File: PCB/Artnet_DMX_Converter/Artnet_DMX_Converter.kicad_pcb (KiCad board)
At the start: 4 copper layers, 100 x 72 mm, 208 parts, among them IC1 NPM1300-QEAA-R7, J1 Conn_01x03_MountingPin, J10 XLR5, J11 XLR3, J12 IDC, J13 Conn_02x04, J2 USB_C_Receptacle_USB2.0_14P, J3 RJ45, J4 XLR5, J5 XLR3, J6 XLR5, J7 XLR3, J8 XLR5, J9 XLR3, SW1 SW_Push, SW2 SW_Push, T1 FA2805, U1 RP2350B, U10 MAX3485, U11 MAX3485, U12 TXS0101DCK, U2 W25Q128JVS, U3 USBLC6-2SC6, U4 W5500, U5 VO618A-3X019T, U6 SI3402-B-GMR, U7 TLV431, U8 MAX3485, U9 MAX3485, Y1 ABM8-272-T3, Y2 ABM8-25.000MHZ-10-D1G-T

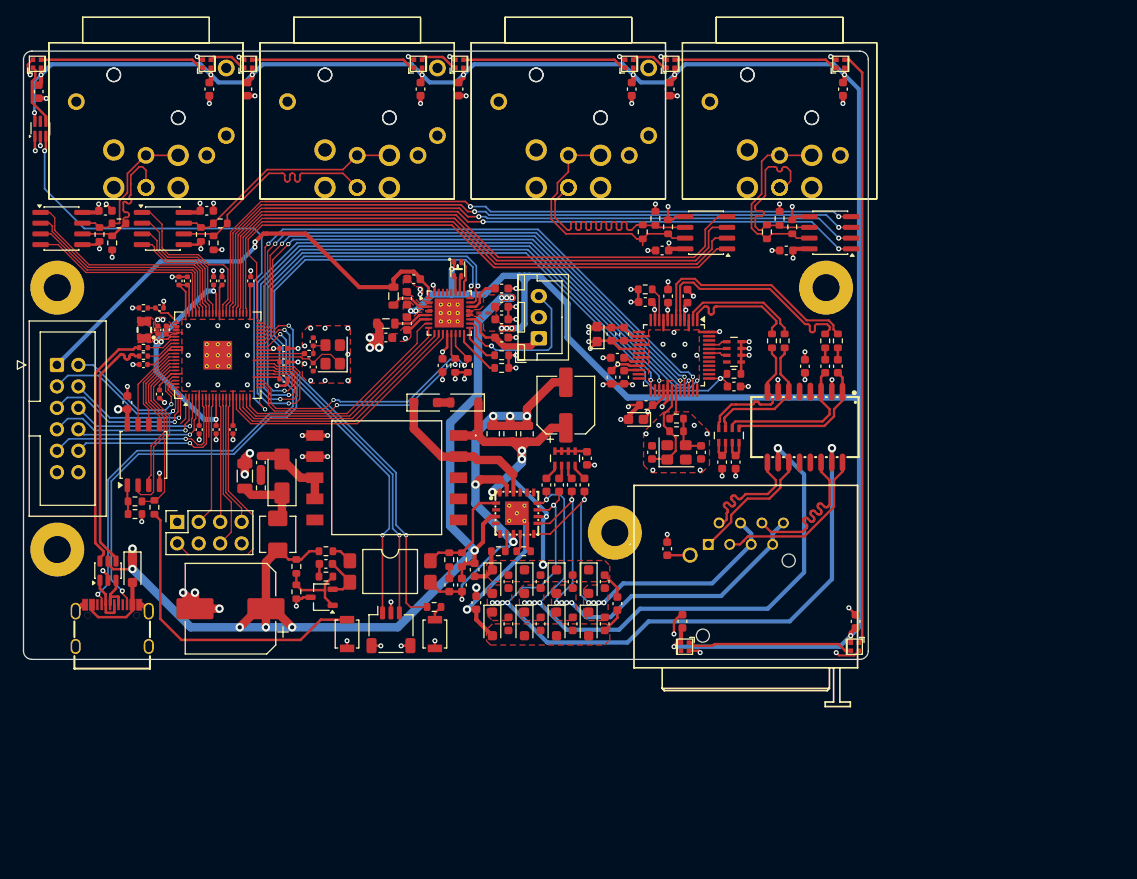
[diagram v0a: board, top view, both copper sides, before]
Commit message: Updated the PCB Allot
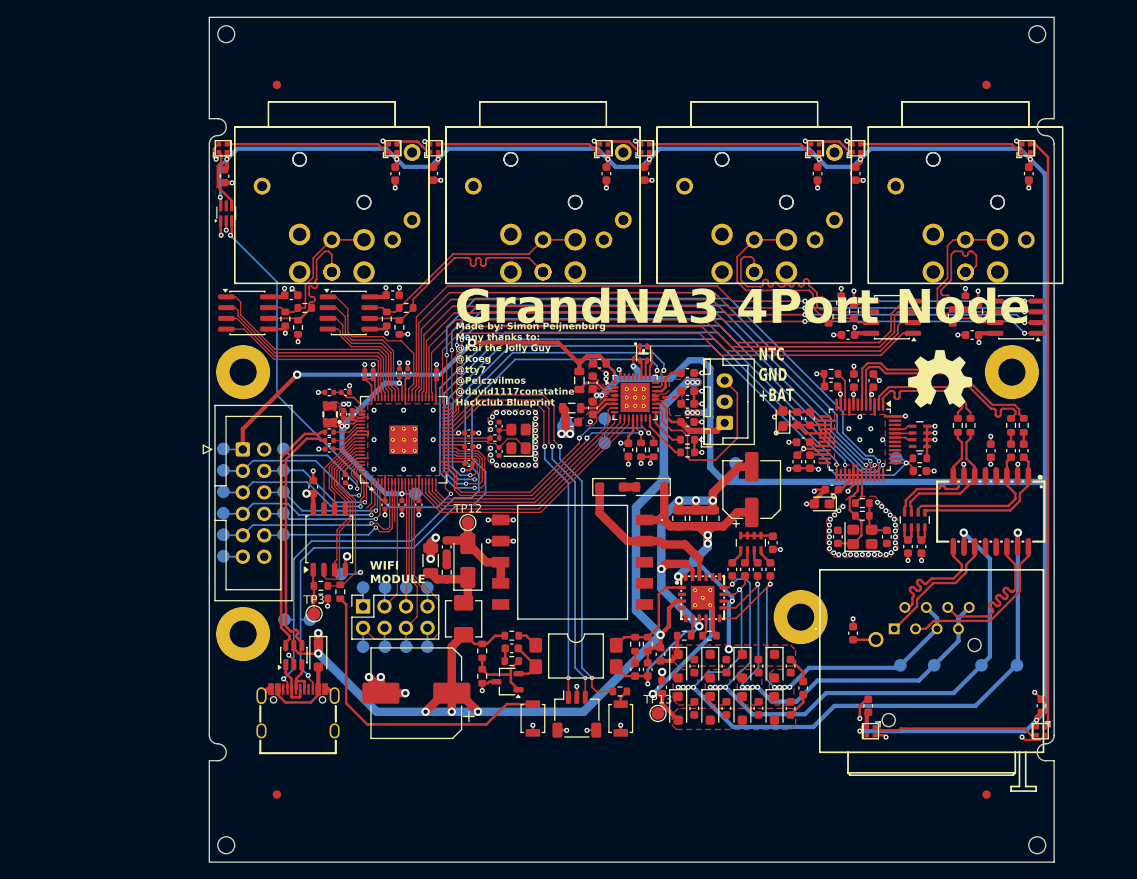
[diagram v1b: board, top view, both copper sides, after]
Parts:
- added FID1: Fiducial, Fiducial:Fiducial_1mm_Mask2mm, F.Cu at (48.0, 34.0)
- added FID2: Fiducial, Fiducial:Fiducial_1mm_Mask2mm, F.Cu at (132.0, 34.0)
- added FID3: Fiducial, Fiducial:Fiducial_1mm_Mask2mm, F.Cu at (48.0, 118.0)
- added FID4: Fiducial, Fiducial:Fiducial_1mm_Mask2mm, F.Cu at (132.0, 118.0)
- added G***: LOGO, Art:Open_source, F.Cu at (126.5, 69.5)
- added G***: LOGO, Art:RAWR, B.Cu at (102.8, 72.5)
- added H5: MountingHole, MountingHole:MountingHole_2mm, F.Cu at (42.0, 28.0)
- added H6: MountingHole, MountingHole:MountingHole_2mm, F.Cu at (138.0, 28.0)
- added H7: MountingHole, MountingHole:MountingHole_2mm, F.Cu at (42.0, 124.0)
- added H8: MountingHole, MountingHole:MountingHole_2mm, F.Cu at (138.0, 124.0)
- added TP1: TestPoint, TestPoint:TestPoint_Pad_D1.5mm, B.Cu at (55.6, 91.9)
- added TP10: TestPoint, TestPoint:TestPoint_Pad_D1.5mm, B.Cu at (121.3, 78.2)
- added TP11: TestPoint, TestPoint:TestPoint_Pad_D1.5mm, B.Cu at (97.5, 90.3)
- added TP12: TestPoint, TestPoint:TestPoint_Pad_D1.5mm, F.Cu at (70.6, 85.8)
- added TP13: TestPoint, TestPoint:TestPoint_Pad_D1.5mm, F.Cu at (93.1, 108.4)
- added TP14: TestPoint, TestPoint:TestPoint_Pad_D1.5mm, B.Cu at (93.8, 80.7)
- added TP15: TestPoint, TestPoint:TestPoint_Pad_D1.5mm, B.Cu at (102.3, 78.8)
- added TP16: TestPoint, TestPoint:TestPoint_Pad_D1.5mm, B.Cu at (82.2, 73.8)
- added TP17: TestPoint, TestPoint:TestPoint_Pad_D1.5mm, B.Cu at (86.8, 73.5)
- added TP18: TestPoint, TestPoint:TestPoint_Pad_D1.5mm, B.Cu at (86.8, 76.4)
- added TP19: TestPoint, TestPoint:TestPoint_Pad_D1.5mm, B.Cu at (41.7, 77.1)
- added TP2: TestPoint, TestPoint:TestPoint_Pad_D1.5mm, B.Cu at (64.4, 82.4)
- added TP20: TestPoint, TestPoint:TestPoint_Pad_D1.5mm, B.Cu at (48.8, 77.1)
- added TP21: TestPoint, TestPoint:TestPoint_Pad_D1.5mm, B.Cu at (41.7, 79.6)
- added TP22: TestPoint, TestPoint:TestPoint_Pad_D1.5mm, B.Cu at (48.8, 79.6)
- added TP23: TestPoint, TestPoint:TestPoint_Pad_D1.5mm, B.Cu at (41.7, 82.2)
- added TP24: TestPoint, TestPoint:TestPoint_Pad_D1.5mm, B.Cu at (48.8, 82.2)
- added TP25: TestPoint, TestPoint:TestPoint_Pad_D1.5mm, B.Cu at (41.7, 84.7)
- added TP26: TestPoint, TestPoint:TestPoint_Pad_D1.5mm, B.Cu at (48.8, 84.7)
- added TP27: TestPoint, TestPoint:TestPoint_Pad_D1.5mm, B.Cu at (41.7, 87.2)
- added TP28: TestPoint, TestPoint:TestPoint_Pad_D1.5mm, B.Cu at (48.8, 87.2)
- added TP29: TestPoint, TestPoint:TestPoint_Pad_D1.5mm, B.Cu at (41.7, 89.8)
- added TP3: TestPoint, TestPoint:TestPoint_Pad_D1.5mm, F.Cu at (52.4, 96.6)
- added TP30: TestPoint, TestPoint:TestPoint_Pad_D1.5mm, B.Cu at (65.8, 93.5)
- added TP31: TestPoint, TestPoint:TestPoint_Pad_D1.5mm, B.Cu at (65.8, 100.5)
- added TP32: TestPoint, TestPoint:TestPoint_Pad_D1.5mm, B.Cu at (63.3, 93.5)
- added TP33: TestPoint, TestPoint:TestPoint_Pad_D1.5mm, B.Cu at (63.3, 100.5)
- added TP34: TestPoint, TestPoint:TestPoint_Pad_D1.5mm, B.Cu at (60.8, 93.5)
- added TP35: TestPoint, TestPoint:TestPoint_Pad_D1.5mm, B.Cu at (60.8, 100.5)
- added TP36: TestPoint, TestPoint:TestPoint_Pad_D1.5mm, B.Cu at (58.2, 93.5)
- added TP37: TestPoint, TestPoint:TestPoint_Pad_D1.5mm, B.Cu at (58.2, 100.5)
- added TP4: TestPoint, TestPoint:TestPoint_Pad_D1.5mm, B.Cu at (51.9, 97.3)
- added TP5: TestPoint, TestPoint:TestPoint_Pad_D1.5mm, B.Cu at (48.9, 97.3)
- added TP6: TestPoint, TestPoint:TestPoint_Pad_D1.5mm, B.Cu at (121.8, 102.7)
- added TP7: TestPoint, TestPoint:TestPoint_Pad_D1.5mm, B.Cu at (125.8, 102.7)
- added TP8: TestPoint, TestPoint:TestPoint_Pad_D1.5mm, B.Cu at (135.6, 102.7)
- added TP9: TestPoint, TestPoint:TestPoint_Pad_D1.5mm, B.Cu at (131.4, 102.7)
- moved C8 24.6 mm to (66.9, 68.3)
- moved C10 24.6 mm to (59.4, 68.3)
- moved C11 24.6 mm to (58.4, 68.3)
- moved C3 24.6 mm to (62.5, 68.1)
- moved C9 24.6 mm to (63.5, 68.1)
- moved C70 24.2 mm to (130.3, 63.6)
- moved C87 24.2 mm to (82.9, 73.9)
- moved C14 24.2 mm to (56.1, 70.4)
- moved C82 24.2 mm to (85.4, 69.2)
- moved C83 24.2 mm to (85.4, 72.2)
- moved C85 24.2 mm to (96.6, 73.9)
- moved L5 24.2 mm to (82.9, 72.2)
- moved R2 24.2 mm to (54.2, 70.4)
- moved U5 24.2 mm to (83.4, 101.6)
- moved U7 24.2 mm to (75.3, 104.7)
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- renumbered C42 to C38, C43 to C39, C44 to C40, C45 to C41, C46 to C42, C38 to C43, C39 to C44, C40 to C45, C41 to C46, H3 to H2, H2 to H3, R12 to R10, R13 to R11, R14 to R12, R15 to R13, R16 to R14, R17 to R15, R18 to R16, R19 to R17, R20 to R18, R21 to R19, R22 to R20, R23 to R21, R24 to R22, R25 to R23, R26 to R24, R27 to R25, R28 to R26, R29 to R27, R30 to R28, R31 to R29, R32 to R30, R33 to R31, R34 to R32, R35 to R33, R36 to R34, R37 to R35, R38 to R36, R39 to R37, R40 to R38, R41 to R39, R42 to R40, R43 to R41, R11 to R9
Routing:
- net /Microcontroller/RUN: track 45.4 -> 52.7 mm
- net /Microcontroller/SWDIO: track 42.7 -> 50.0 mm
- net /Microcontroller/SWCLK: track 41.7 -> 48.3 mm
- net /DMX/LEDs: track 58.6 -> 52.6 mm
- net /DMX/DMX_2_RDM: track 70.8 -> 65.6 mm
- net /POWER/CC2: track 85.0 -> 79.8 mm
- net Net-(BT1-NTC): track 18.4 -> 22.9 mm, vias 1 -> 0
- net /Ethernet/MOSI: track 70.3 -> 74.2 mm
- net +1V1: track 48.8 -> 45.0 mm
- net /DMX/2_RDM_EN: track 70.6 -> 66.8 mm
- net /POWER/CC1: track 87.4 -> 83.7 mm
- net /DMX/DMX_2_EN: track 72.1 -> 68.8 mm
- net /Microcontroller/QSPI_SS: track 20.1 -> 23.1 mm, vias 0 -> 1
- net /Ethernet/SCK: track 68.9 -> 71.8 mm
- net /Ethernet/LINKLED: track 78.3 -> 75.5 mm
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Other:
- board size 100 x 72 mm -> 100 x 100 mm
- board text added: "BCKLGHT 3V3 MOSI RST RS SCLK ENC_SW CS ENC_B ENC_A GND GND"
- board text added: "GND RX IO11 EN IO12 RST TX 3V3"
- board text added: "GrandNA3 4Port Node"
- board text added: "Made by: Simon Peijnenburg Many thanks to: @Kai the Jolly Guy @Koeg @tty7 @Pelczvilmos @david1117constatine Hackclub Blueprint"
- board text added: "NTC GND +BAT"
- board text added: "SWCLK GND SWDIO"
- board text added: "V-CUT"
- board text added: "WIFI MODULE"
